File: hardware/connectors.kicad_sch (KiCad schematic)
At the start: 4 parts, among them J1 USB_B_Micro, J2 SWD Connector, J3 PWR, U3 USBLC6-2SC6

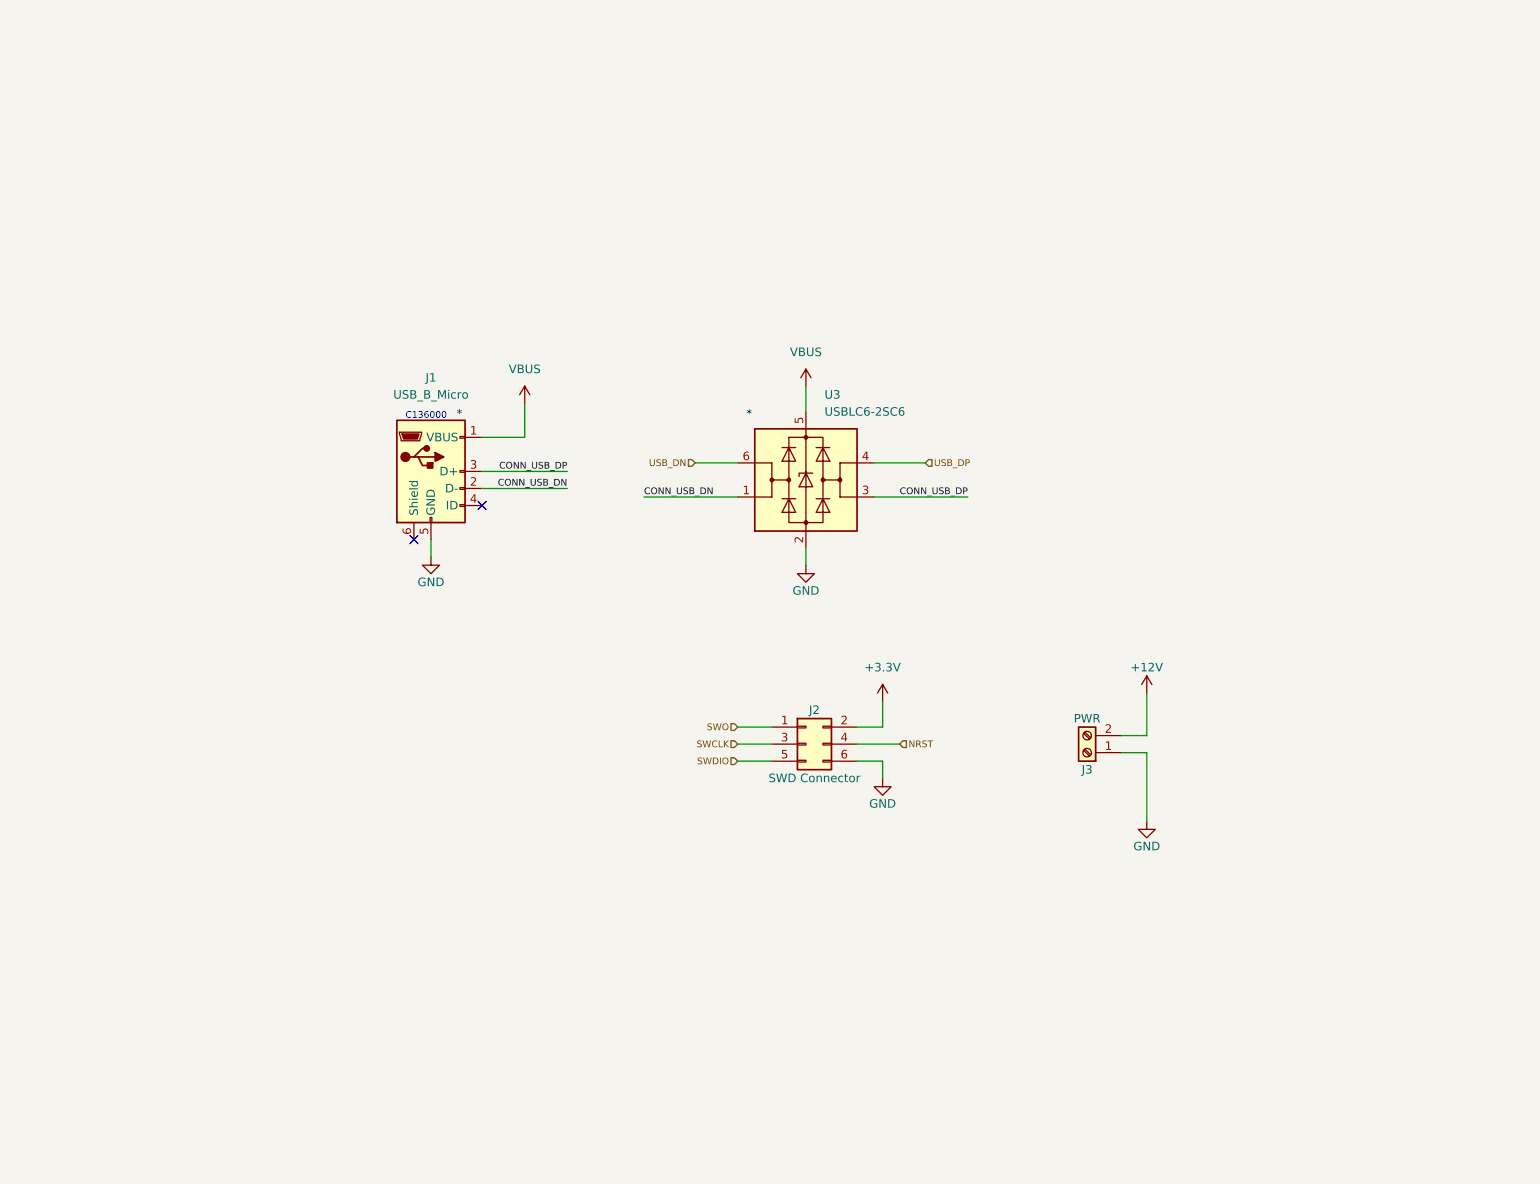
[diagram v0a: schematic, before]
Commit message: Moved hardware to separate directory
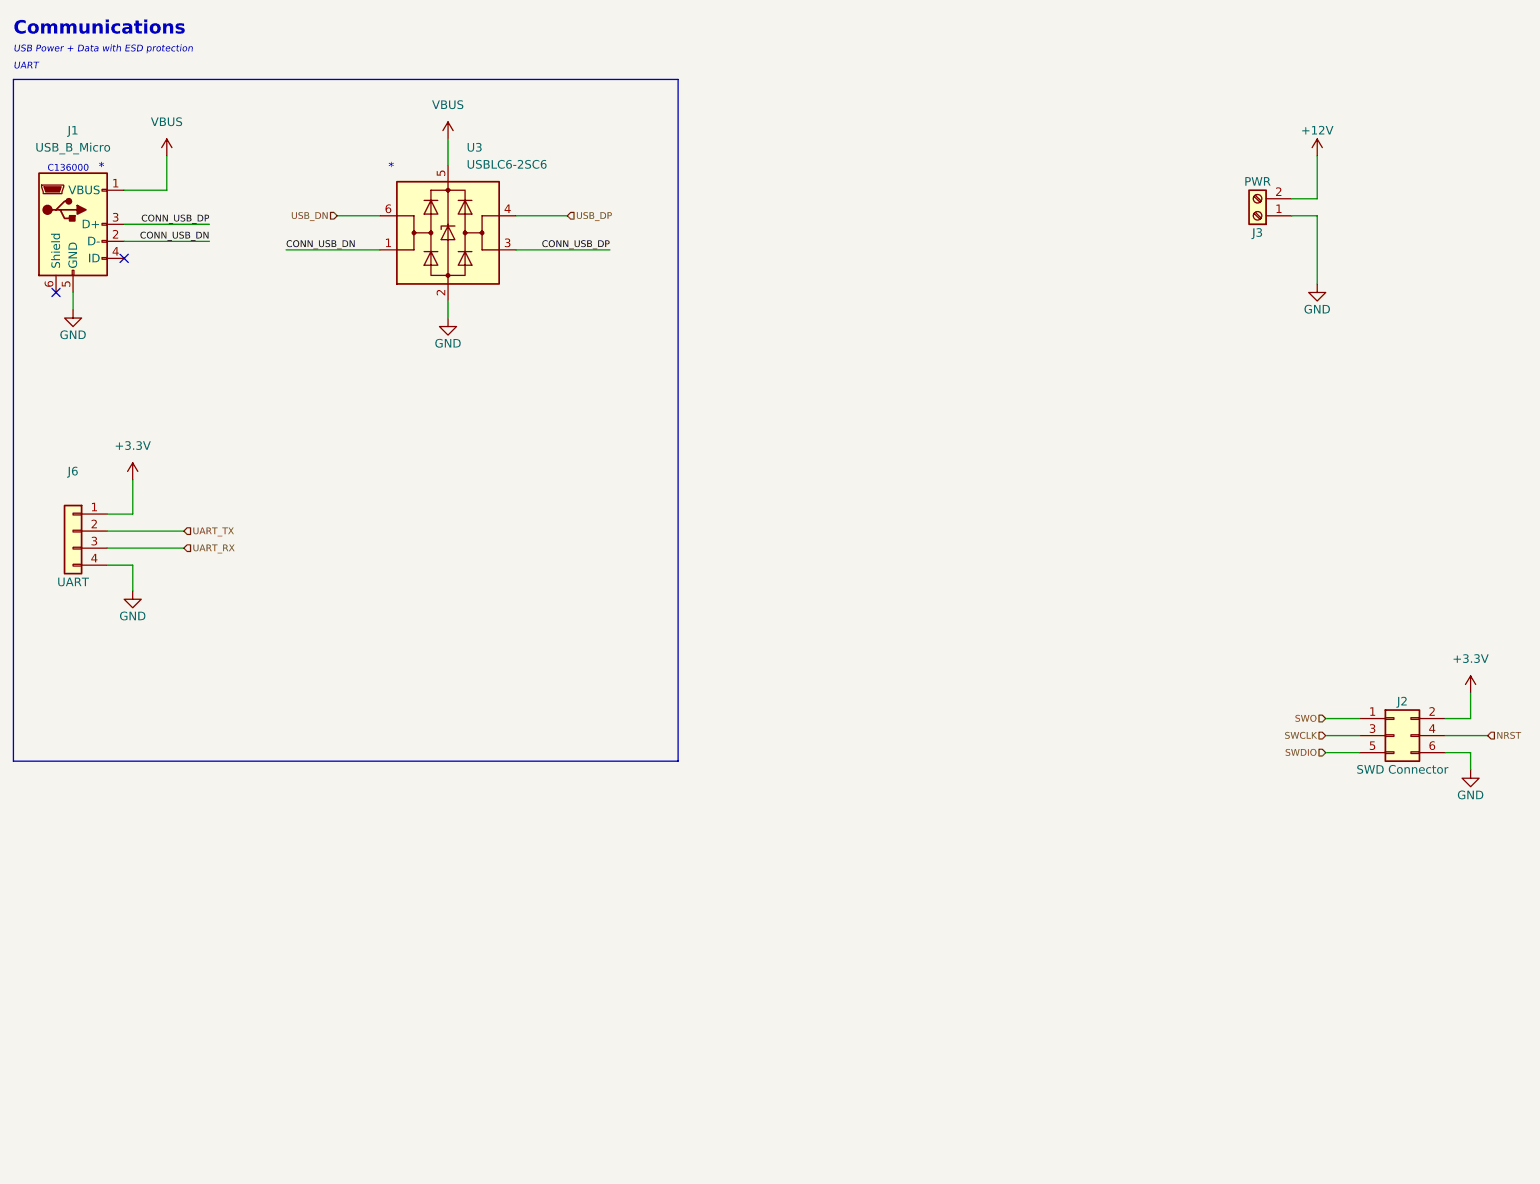
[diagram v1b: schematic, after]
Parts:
- added J6: UART, symbol Connector_Generic:Conn_01x04
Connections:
- net +3.3V: now also J6.1 (Pin_1)
- net GND: now also J6.4 (Pin_4)
- new net UART_RX: J6.3 (Pin_3)
- new net UART_TX: J6.2 (Pin_2)
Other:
- note added: "Communications"
- note added: "UART"
- note added: "USB Power + Data with ESD protection"
- company: (none) -> Sampreet SARKAR
- moved on the sheet: J1, J2, J3, U3

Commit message: Added pin assignments in firmware
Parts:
- J6: footprint (none) -> Connector_JST:JST_PH_S4B-PH-K_1x04_P2.00mm_Horizontal
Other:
- title: (none) -> Posit: A STM32 based DC motor controller
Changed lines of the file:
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@@
   (paper "A4")
   (title_block
+    (title "Posit: A STM32 based DC motor controller")
     (rev "A")
     (company "Sampreet SARKAR")
@@
     (property "Reference" "J6" (id 0) (at 24.13 91.44 0))
     (property "Value" "UART" (id 1) (at 24.13 107.95 0))
-    (property "Footprint" "" (id 2) (at 24.13 100.33 0)
-      (effects (font (size 1.27 1.27)) hide)
-    )
+    (property "Footprint" "Connector_JST:JST_PH_S4B-PH-K_1x04_P2.00mm_Horizontal" (id 2) (at 24.13 100.33 0)
+      (effects (font (size 1.27 1.27)) hide)
+    )

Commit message: Added LEDs and UART
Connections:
- net UART_RX: now also J6.2 (Pin_2); no longer J6.3 (Pin_3)
- net UART_TX: now also J6.3 (Pin_3); no longer J6.2 (Pin_2)
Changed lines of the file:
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@@
     (effects (font (size 1 1)) (justify left))
   )
-  (hierarchical_label "UART_RX" (shape input) (at 40.64 102.87 0)
+  (hierarchical_label "UART_RX" (shape input) (at 40.64 100.33 0)
     (effects (font (size 1 1)) (justify left))
   )
@@
     (effects (font (size 1 1)) (justify right))
   )
-  (hierarchical_label "UART_TX" (shape input) (at 40.64 100.33 0)
+  (hierarchical_label "UART_TX" (shape input) (at 40.64 102.87 0)
     (effects (font (size 1 1)) (justify left))
   )

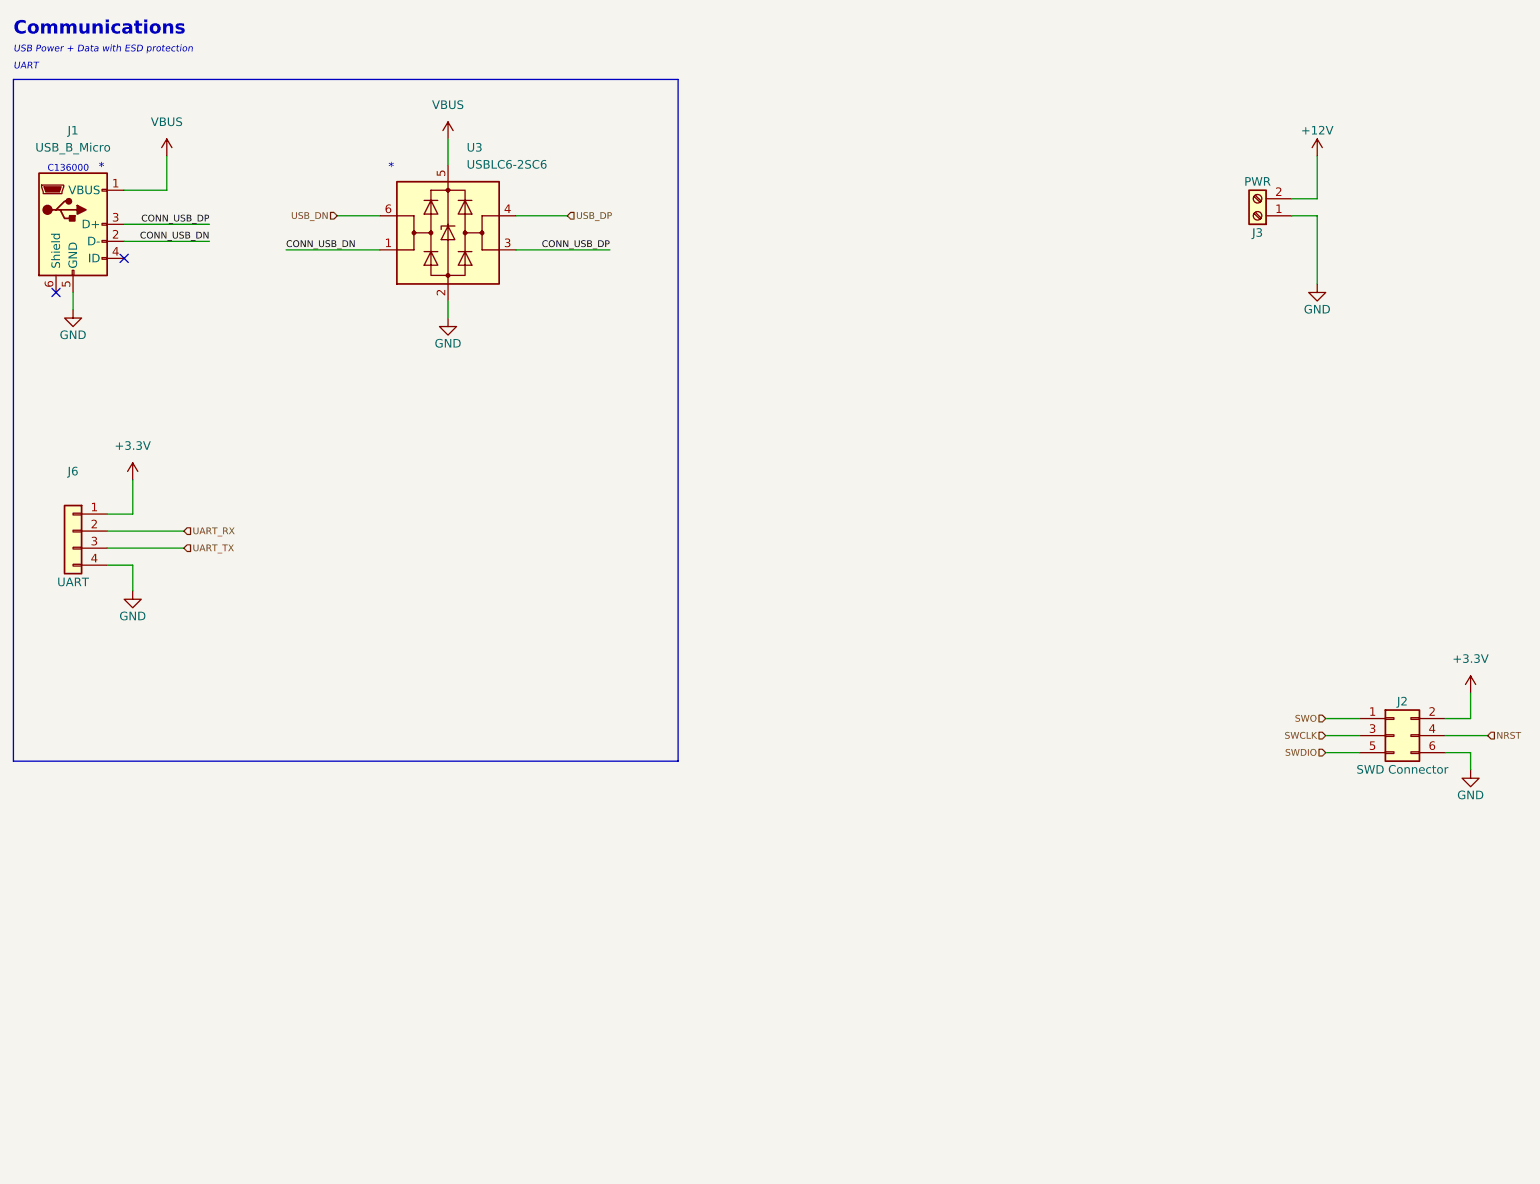
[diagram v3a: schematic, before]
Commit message: Updated hardware design, added TagConnect Probe and Battery Voltage Measurement
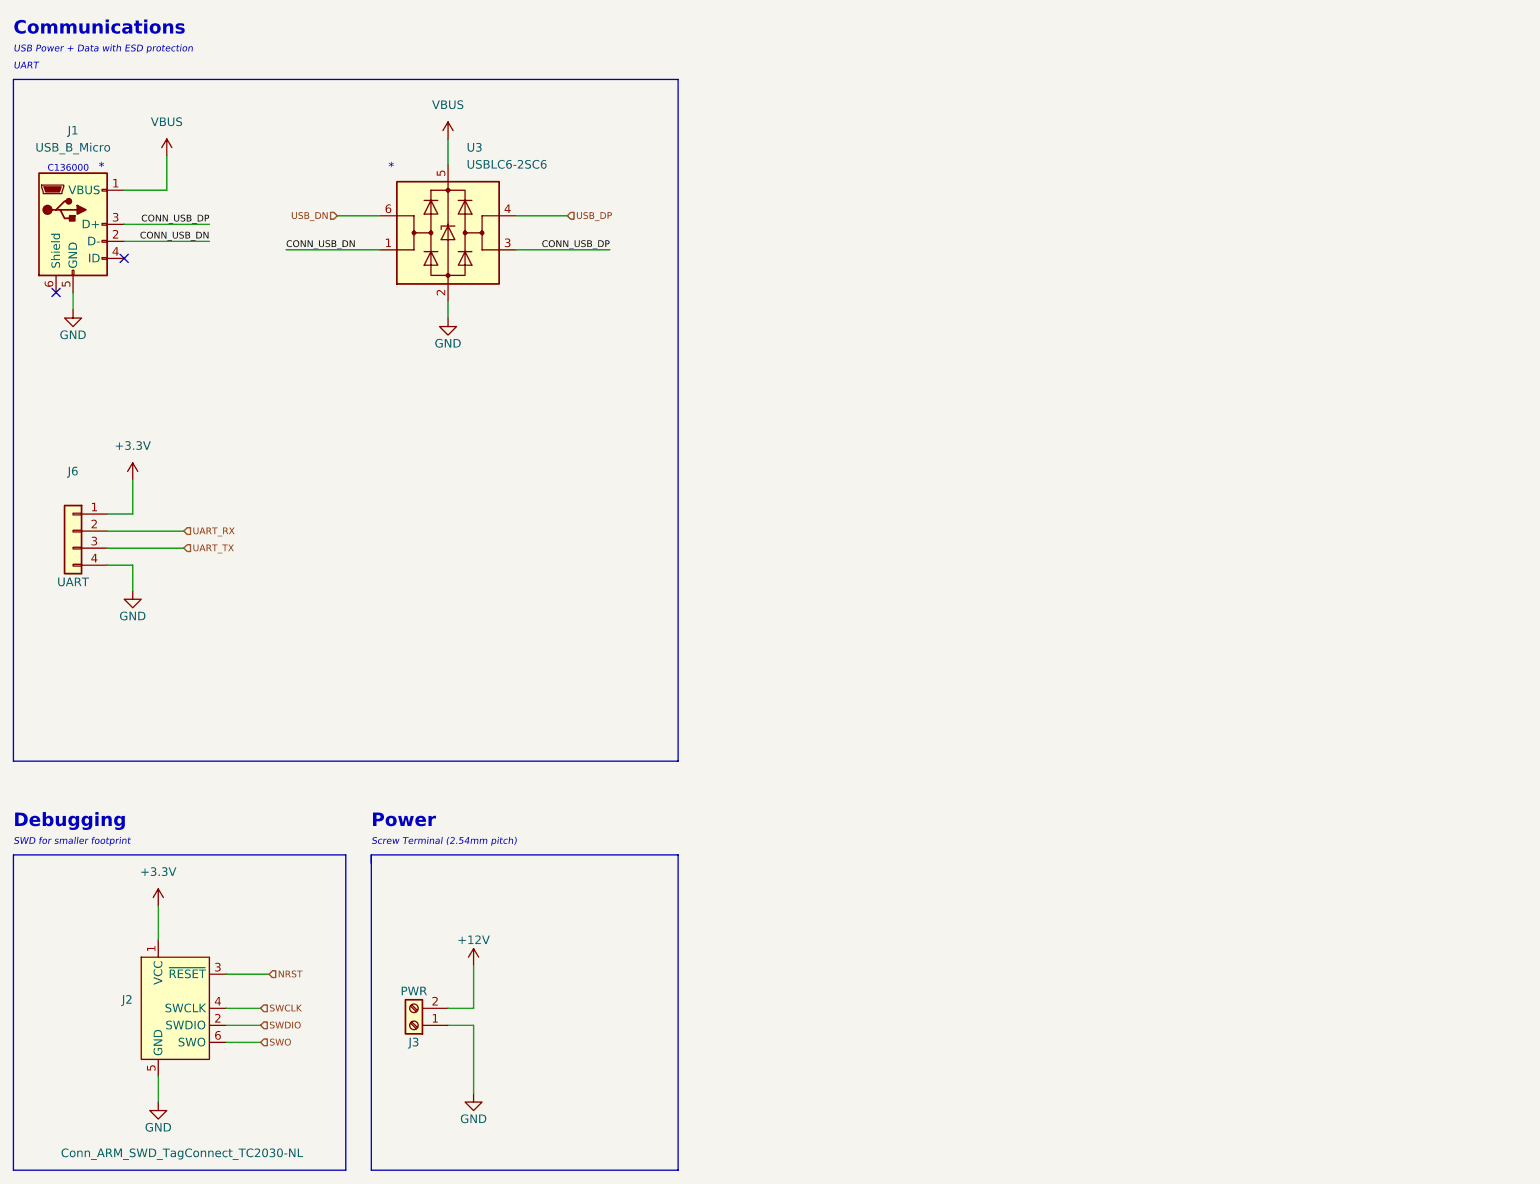
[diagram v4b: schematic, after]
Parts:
- removed J2: SWD Connector, Connector_PinHeader_2.54mm:PinHeader_2x03_P2.54mm_Vertical, symbol Connector_Generic:Conn_02x03_Odd_Even
- added J2: Conn_ARM_SWD_TagConnect_TC2030-NL, Connector:Tag-Connect_TC2030-IDC-NL_2x03_P1.27mm_Vertical, symbol Connector:Conn_ARM_SWD_TagConnect_TC2030-NL
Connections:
- net +3.3V: now also J2.1 (VCC)
- net GND: now also J2.5 (GND)
- net NRST: now also J2.3 (~{RESET})
- net SWCLK: now also J2.4 (SWCLK)
- net SWDIO: now also J2.2 (SWDIO)
- net SWO: now also J2.6 (SWO)
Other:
- note added: "Debugging"
- note added: "Power"
- note added: "SWD for smaller footprint"
- note added: "Screw Terminal (2.54mm pitch)"
- moved on the sheet: J3
